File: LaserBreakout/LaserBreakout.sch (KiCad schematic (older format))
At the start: 7 parts, among them J1 LASER_CONN, J2 949, J3 MiniFitPower

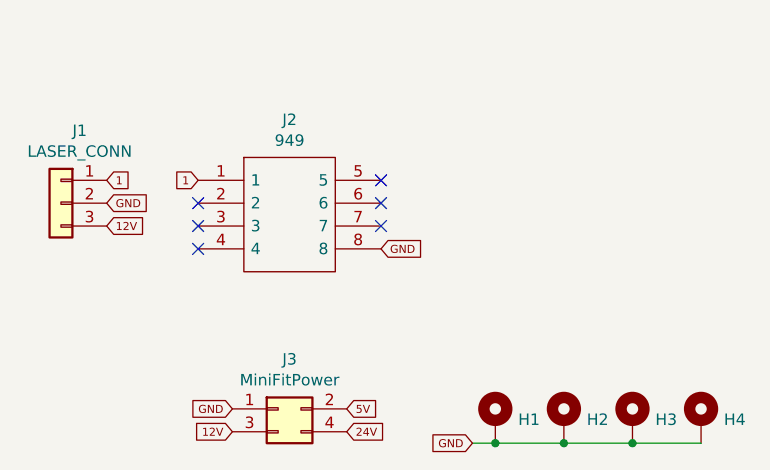
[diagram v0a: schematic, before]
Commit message: Add more breakout boards
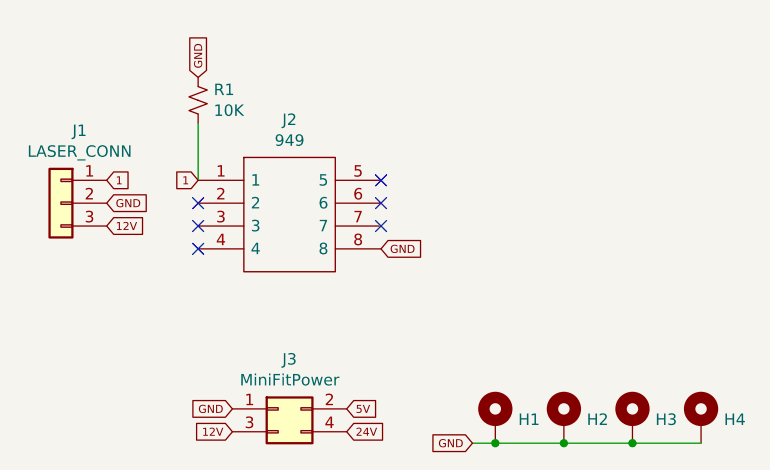
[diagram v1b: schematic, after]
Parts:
- added R1: 10K, Resistor_THT:R_Axial_DIN0204_L3.6mm_D1.6mm_P5.08mm_Horizontal, symbol Device:R_Small_US
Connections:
- net 1: now also R1.2
- net GND: now also R1.1
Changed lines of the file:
@@
 NoConn ~ 3100 3750
 NoConn ~ 3100 3650
+$Comp
+L Device:R_Small_US R1
+U 1 1 5EA20099
+P 3100 3200
+F 0 "R1" H 3168 3246 50  0000 L CNN
+F 1 "10K" H 3168 3155 50  0000 L CNN
+F 2 "Resistor_THT:R_Axial_DIN0204_L3.6mm_D1.6mm_P5.08mm_Horizontal" H 3100 3200 50  0001 C CNN
+F 3 "~" H 3100 3200 50  0001 C CNN
+	1    3100 3200
+	1    0    0    -1
+$EndComp
+Text GLabel 3100 3100 1    35   Input ~ 0
+GND
+Wire Wire Line
+	3100 3300 3100 3550
 $EndSCHEMATC

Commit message: So many things
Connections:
- net 2: now reaches J2.2
- net 2: now also J1.1 (Pin_1), R1.2
- removed net 1: J1.1 (Pin_1), J2.1, R1.2
- no-connect marks 6 -> 5
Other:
- moved on the sheet: R1
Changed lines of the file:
@@
 	1    0    0    -1
 $EndComp
-Text GLabel 3100 3550 0    35   Input ~ 0
-1
+Text GLabel 3000 3650 0    35   Input ~ 0
+2
 Text GLabel 3900 3850 2    35   Input ~ 0
 GND
@@
 $EndComp
 Text GLabel 2700 3550 2    35   Input ~ 0
-1
+2
 Text GLabel 2700 3650 2    35   Input ~ 0
 GND
@@
 NoConn ~ 3100 3850
 NoConn ~ 3100 3750
-NoConn ~ 3100 3650
 $Comp
 L Device:R_Small_US R1
 U 1 1 5EA20099
-P 3100 3200
-F 0 "R1" H 3168 3246 50  0000 L CNN
-F 1 "10K" H 3168 3155 50  0000 L CNN
-F 2 "Resistor_THT:R_Axial_DIN0204_L3.6mm_D1.6mm_P5.08mm_Horizontal" H 3100 3200 50  0001 C CNN
-F 3 "~" H 3100 3200 50  0001 C CNN
-	1    3100 3200
+P 3000 3150
+F 0 "R1" H 3068 3196 50  0000 L CNN
+F 1 "10K" H 3068 3105 50  0000 L CNN
+F 2 "Resistor_THT:R_Axial_DIN0204_L3.6mm_D1.6mm_P5.08mm_Horizontal" H 3000 3150 50  0001 C CNN
+F 3 "~" H 3000 3150 50  0001 C CNN
+	1    3000 3150
 	1    0    0    -1
 $EndComp
-Text GLabel 3100 3100 1    35   Input ~ 0
+Text GLabel 3000 3050 1    35   Input ~ 0
 GND
 Wire Wire Line
-	3100 3300 3100 3550
+	3000 3250 3000 3650
+Wire Wire Line
+	3000 3650 3100 3650
 $EndSCHEMATC
